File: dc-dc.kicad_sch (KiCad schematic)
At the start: 137 parts, among them SW3 CVS-02B, U31 MPM54304GMN, U32 MPM54304GMN, U33 MAX16150AUT+T, U34 NCP451AFCT2G, U35 SN74LVC1G125DBVR, U36 LM3880, U37 MP8869S, U38 TPS7A20185PDQNR, U39 NCP51400MNTXG, U40 XC6230H001ER-G, U41 REF3012AIDBZT, U44 NCP718BSN330T1G, U47 74LVC1T45GM

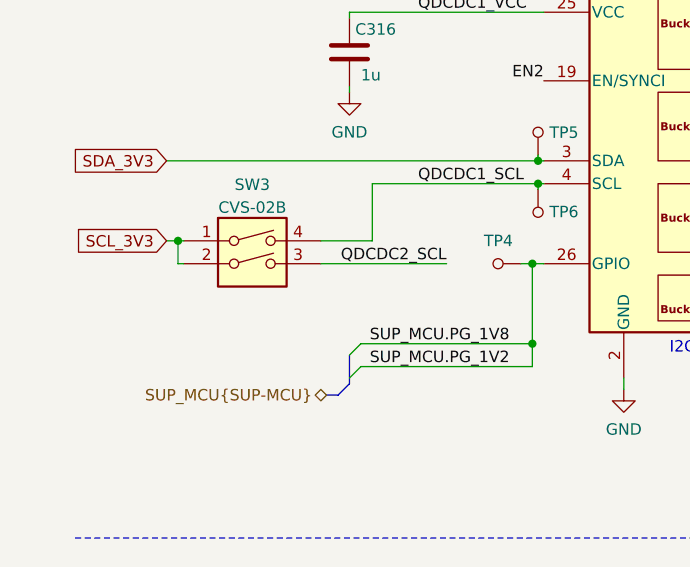
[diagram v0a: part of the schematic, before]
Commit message: Updated all symbols causing warnings with no signal connected to pad, added thermal vias on level shifters' thermal pad with small tweaks on signal routing near this area
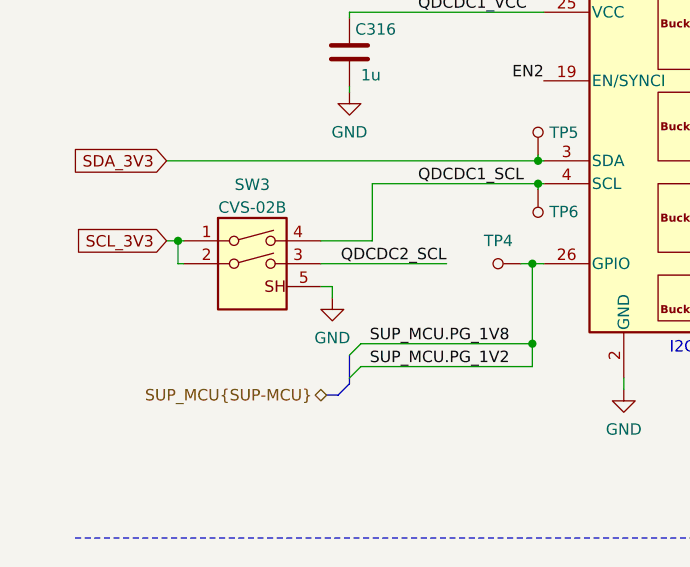
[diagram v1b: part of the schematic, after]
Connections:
- net GND: now also SW3.5 (SH)
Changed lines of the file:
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@@
     (stroke (width 0) (type default) (color 0 0 0 0))
   )
+  (wire (pts (xy 47.625 143.51) (xy 47.625 144.78))
+    (stroke (width 0) (type default) (color 0 0 0 0))
+  )
   (wire (pts (xy 377.19 161.29) (xy 377.19 163.83))
     (stroke (width 0) (type default) (color 0 0 0 0))
@@
     (stroke (width 0) (type default) (color 0 0 0 0))
   )
+  (wire (pts (xy 46.355 143.51) (xy 47.625 143.51))
+    (stroke (width 0) (type default) (color 0 0 0 0))
+  )
   (wire (pts (xy 144.78 258.445) (xy 150.495 258.445))
     (stroke (width 0) (type default) (color 0 0 0 0))
@@
     (pin "2")
   )
+  (symbol (lib_id "K410T-devboard:GND") (at 47.625 144.78 0) (unit 1)
+    (in_bom yes) (on_board yes) (fields_autoplaced)
+    (property "Reference" "#PWR0357" (id 0) (at 47.625 151.13 0)
+      (effects (font (size 1.27 1.27)) hide)
+    )
+    (property "Value" "GND" (id 1) (at 47.625 149.2234 0))
+    (property "Footprint" "" (id 2) (at 47.625 144.78 0)
+      (effects (font (size 1.27 1.27)) hide)
+    )
+    (property "Datasheet" "" (id 3) (at 47.625 144.78 0)
+      (effects (font (size 1.27 1.27)) hide)
+    )
+    (pin "1")
+  )
   (symbol (lib_id "K410T-devboard:VDC") (at 281.305 28.575 0) (unit 1)
     (in_bom yes) (on_board yes) (fields_autoplaced)
@@
     )
     (pin "1")
+    (pin "2")
     (pin "3")
   )
@@
     (pin "2")
     (pin "3")
+    (pin "4")
     (pin "5")
   )
@@
     (pin "3")
     (pin "4")
+    (pin "5")
   )
   (symbol (lib_id "K410T-devboard:GND") (at 355.6 245.11 0) (unit 1)
